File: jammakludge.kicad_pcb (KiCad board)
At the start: 2 copper layers, 31 parts, among them J1 Conn_02x28_Odd_Even, J2 Conn_02x28, J3 Conn_02x28

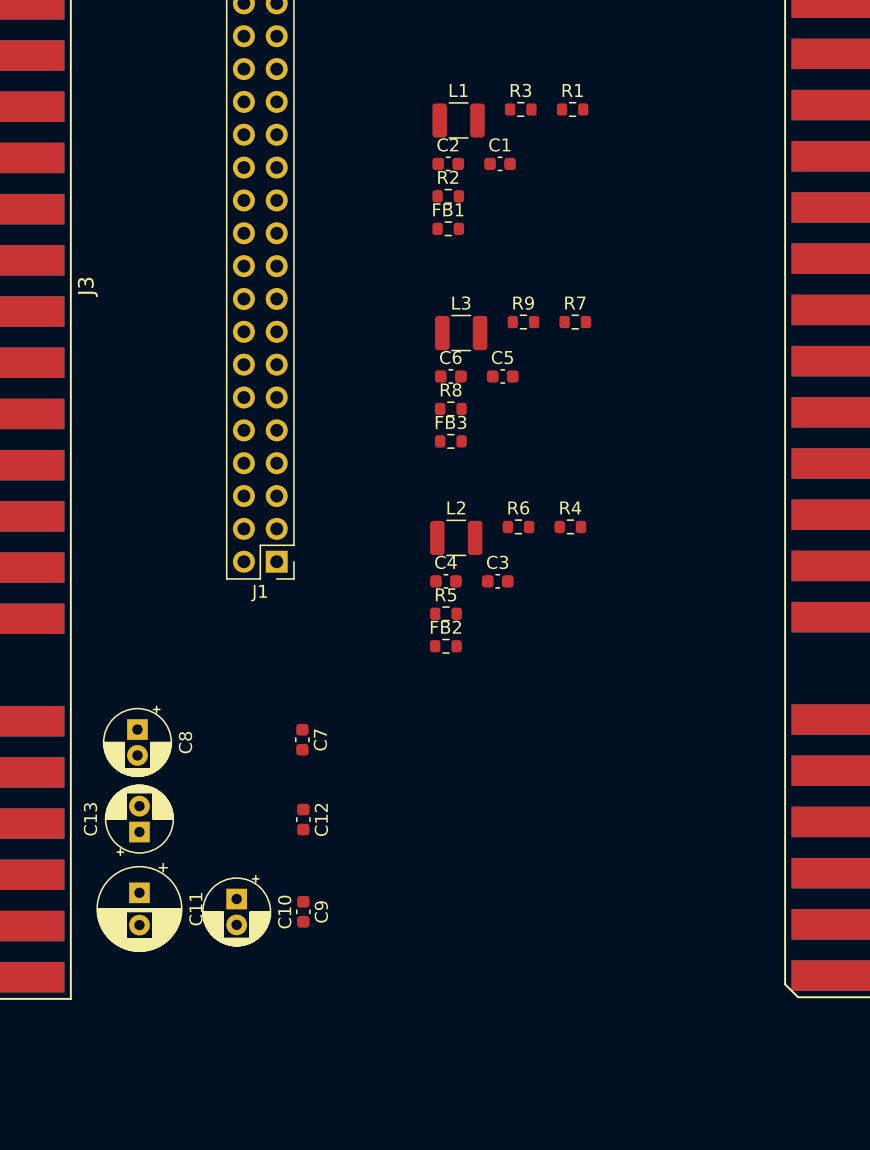
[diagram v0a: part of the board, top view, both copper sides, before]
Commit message: Added more power bypassing capacitors to 5v and 12v supplies.
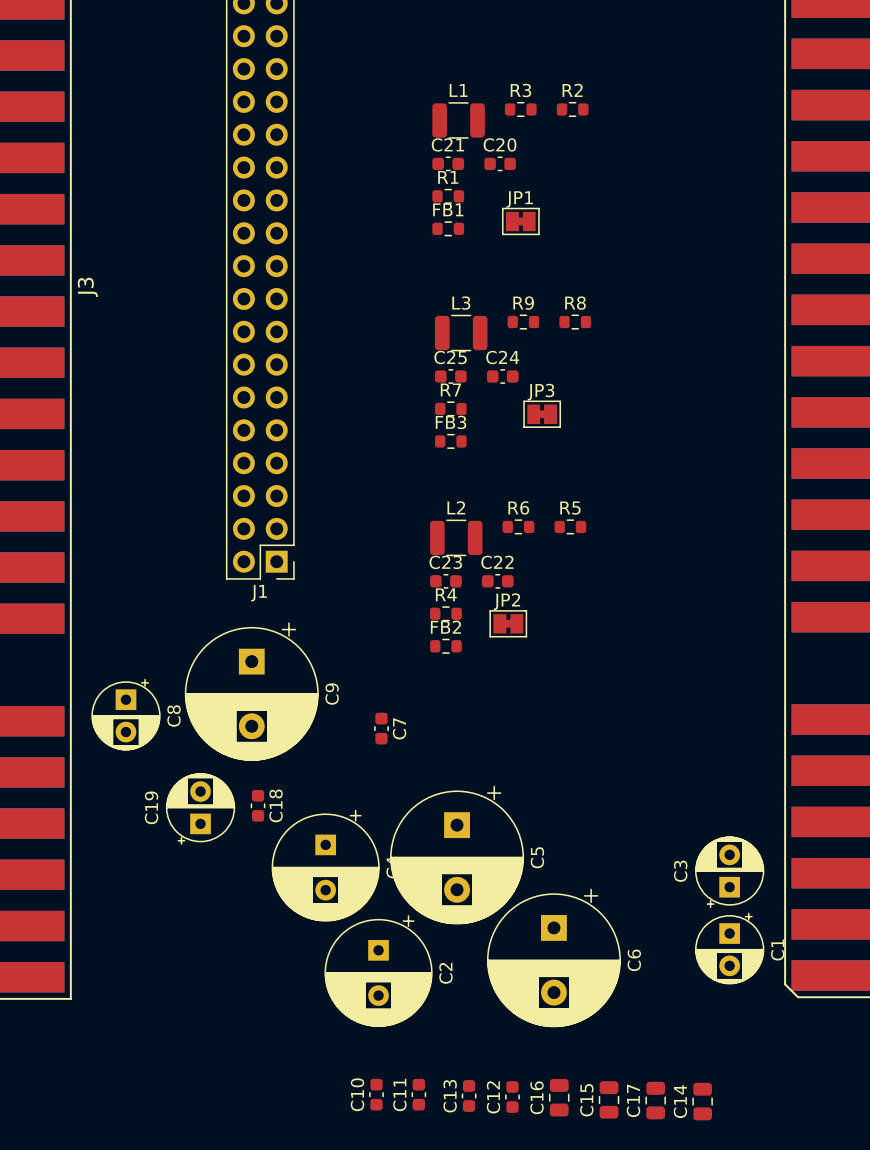
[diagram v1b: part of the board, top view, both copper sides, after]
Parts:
- added C11: C, Capacitor_SMD:C_0603_1608Metric, F.Cu at (56.3, 194.2)
- added C12: C, Capacitor_SMD:C_0603_1608Metric, F.Cu at (63.5, 194.4)
- added C13: C, Capacitor_SMD:C_0603_1608Metric, F.Cu at (60.2, 194.3)
- added C14: C, Capacitor_SMD:C_0805_2012Metric, F.Cu at (78.2, 194.7)
- added C15: C, Capacitor_SMD:C_0805_2012Metric, F.Cu at (71.0, 194.6)
- added C16: C, Capacitor_SMD:C_0805_2012Metric, F.Cu at (67.1, 194.4)
- added C17: C, Capacitor_SMD:C_0805_2012Metric, F.Cu at (74.6, 194.7)
- added C3: C_Polarized, Capacitor_THT:CP_Radial_D5.0mm_P2.50mm, F.Cu at (80.3, 178.2)
- added C4: C_Polarized, Capacitor_THT:CP_Radial_D8.0mm_P3.50mm, F.Cu at (49.1, 174.9)
- added C5: C_Polarized, Capacitor_THT:CP_Radial_D10.0mm_P5.00mm, F.Cu at (59.2, 173.4)
- added C6: C_Polarized, Capacitor_THT:CP_Radial_D10.0mm_P5.00mm, F.Cu at (66.7, 181.3)
- added C9: C_Polarized, Capacitor_THT:CP_Radial_D10.0mm_P5.00mm, F.Cu at (43.4, 160.7)
- added JP1: SolderJumper_2_Bridged, Jumper:SolderJumper-2_P1.3mm_Bridged_Pad1.0x1.5mm, F.Cu at (64.2, 126.7)
- added JP2: SolderJumper_2_Bridged, Jumper:SolderJumper-2_P1.3mm_Bridged_Pad1.0x1.5mm, F.Cu at (63.2, 157.8)
- added JP3: SolderJumper_2_Bridged, Jumper:SolderJumper-2_P1.3mm_Bridged_Pad1.0x1.5mm, F.Cu at (65.8, 141.6)
- C1: renamed from C10; footprint Capacitor_THT:CP_Radial_D5.0mm_P2.00mm -> Capacitor_THT:CP_Radial_D5.0mm_P2.50mm
- C19: renamed from C13; footprint Capacitor_THT:CP_Radial_D5.0mm_P2.00mm -> Capacitor_THT:CP_Radial_D5.0mm_P2.50mm
- C2: renamed from C11; footprint Capacitor_THT:CP_Radial_D6.3mm_P2.50mm -> Capacitor_THT:CP_Radial_D8.0mm_P3.50mm
- C8: footprint Capacitor_THT:CP_Radial_D5.0mm_P2.00mm -> Capacitor_THT:CP_Radial_D5.0mm_P2.50mm
- moved C1 38.2 mm to (80.3, 181.7)
- moved C2 19.0 mm to (53.2, 183.0)
- moved C10 15.2 mm to (53.0, 194.2), turned to 90 degrees
- moved C7 6.18 mm to (53.4, 165.9)
- moved C19 4.77 mm to (39.4, 173.3)
- moved C18 3.66 mm to (43.8, 171.9)
- moved C8 2.47 mm to (33.6, 163.7)
- renumbered C9 to C10, C12 to C18, C1 to C20, C2 to C21, C3 to C22, C4 to C23, C5 to C24, C6 to C25, R2 to R1, R1 to R2, R5 to R4, R4 to R5, R8 to R7, R7 to R8

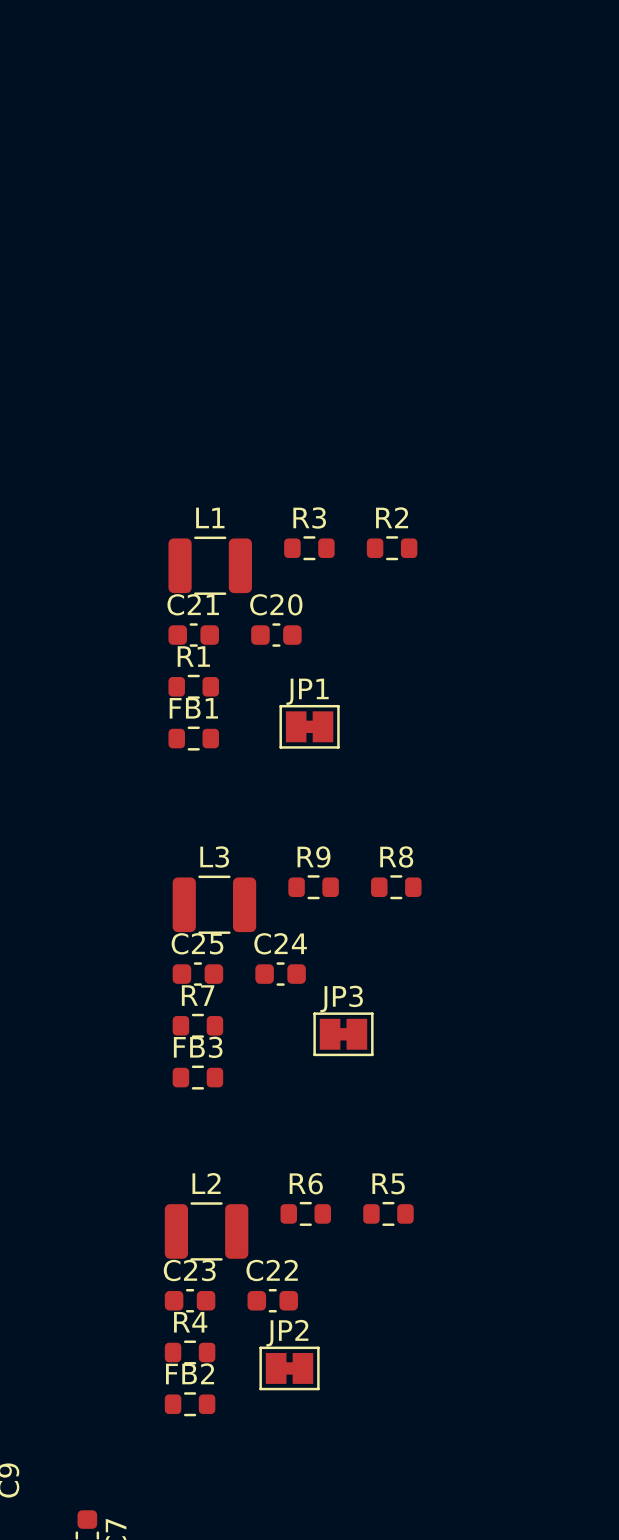
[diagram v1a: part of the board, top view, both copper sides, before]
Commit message: Added test points/breakout points for video filter input and output
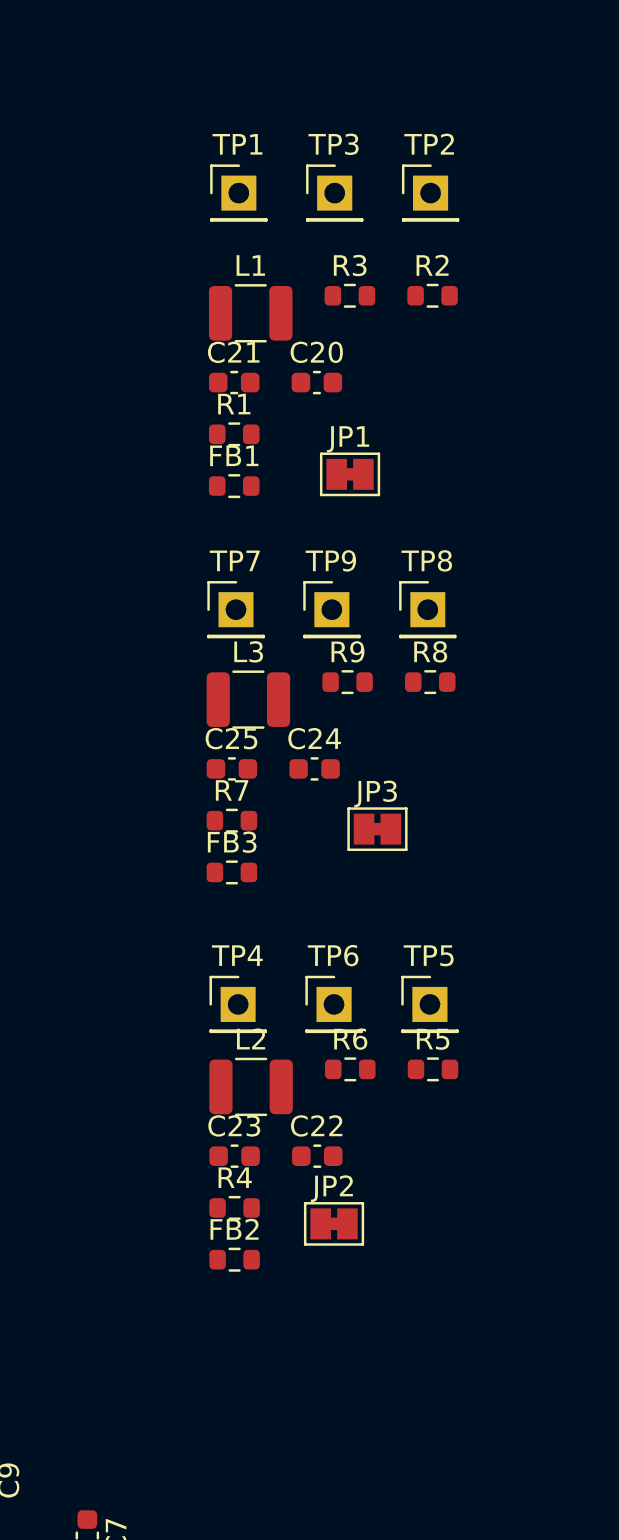
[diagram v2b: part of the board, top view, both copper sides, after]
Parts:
- added TP1: TestPoint, Connector_PinHeader_2.54mm:PinHeader_1x01_P2.54mm_Vertical, F.Cu at (60.7, 100.8)
- added TP2: TestPoint, Connector_PinHeader_2.54mm:PinHeader_1x01_P2.54mm_Vertical, F.Cu at (70.0, 100.8)
- added TP3: TestPoint, Connector_PinHeader_2.54mm:PinHeader_1x01_P2.54mm_Vertical, F.Cu at (65.4, 100.8)
- added TP4: TestPoint, Connector_PinHeader_2.54mm:PinHeader_1x01_P2.54mm_Vertical, F.Cu at (60.7, 140.1)
- added TP5: TestPoint, Connector_PinHeader_2.54mm:PinHeader_1x01_P2.54mm_Vertical, F.Cu at (70.0, 140.1)
- added TP6: TestPoint, Connector_PinHeader_2.54mm:PinHeader_1x01_P2.54mm_Vertical, F.Cu at (65.4, 140.1)
- added TP7: TestPoint, Connector_PinHeader_2.54mm:PinHeader_1x01_P2.54mm_Vertical, F.Cu at (60.6, 121.0)
- added TP8: TestPoint, Connector_PinHeader_2.54mm:PinHeader_1x01_P2.54mm_Vertical, F.Cu at (69.9, 121.0)
- added TP9: TestPoint, Connector_PinHeader_2.54mm:PinHeader_1x01_P2.54mm_Vertical, F.Cu at (65.2, 121.0)
- moved C20 12.4 mm to (64.5, 110.0)
- moved C21 12.4 mm to (60.5, 110.0)
- moved FB1 12.4 mm to (60.5, 115.0)
- moved L1 12.4 mm to (61.3, 106.6)
- moved JP1 12.4 mm to (66.1, 114.4)
- moved R1 12.4 mm to (60.5, 112.5)
- moved R2 12.4 mm to (70.1, 105.8)
- moved R3 12.4 mm to (66.1, 105.8)
- moved C25 10.1 mm to (60.4, 128.7)
- moved FB3 10.1 mm to (60.4, 133.7)
- moved R7 10.1 mm to (60.4, 131.2)
- moved R9 10.1 mm to (66.0, 124.5)
- moved C24 10.1 mm to (64.4, 128.7)
- moved JP3 10.1 mm to (67.5, 131.6)
- moved L3 10.1 mm to (61.2, 125.4)
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
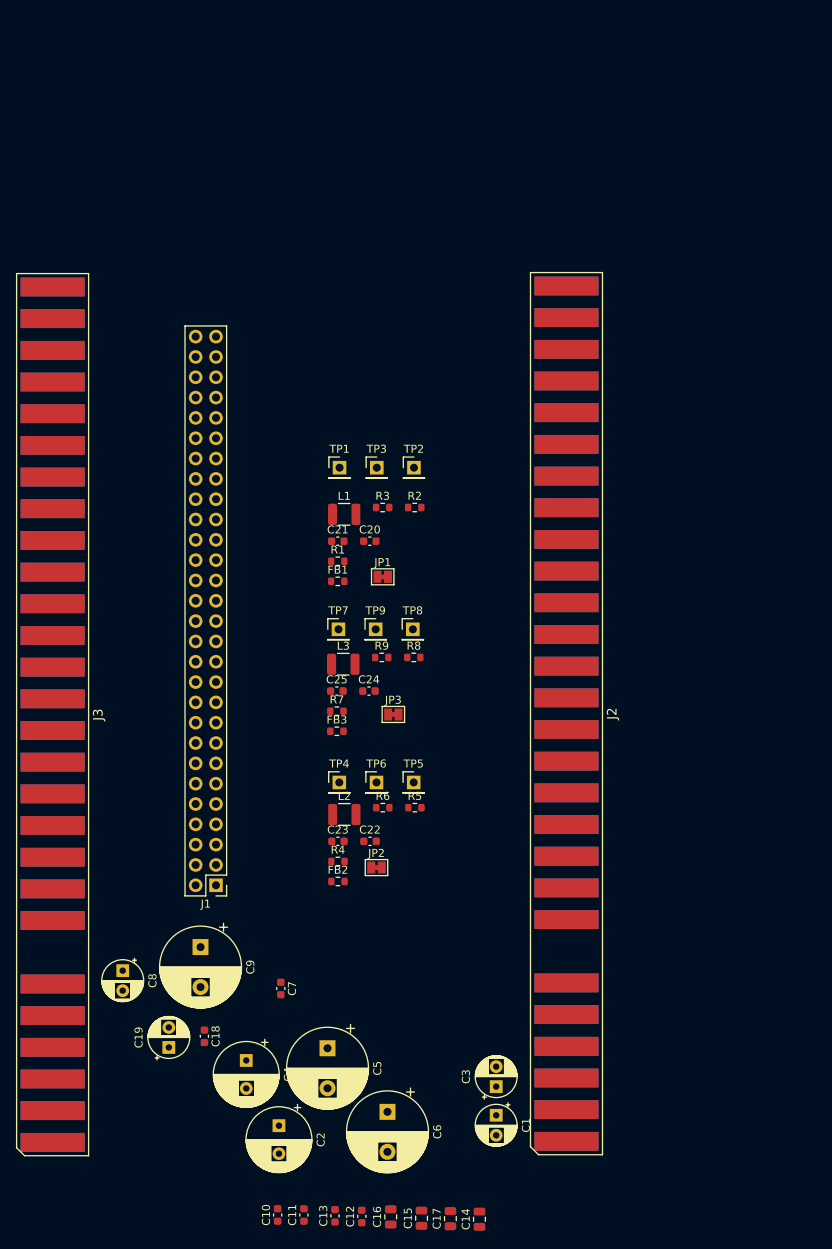
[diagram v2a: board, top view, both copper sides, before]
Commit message: Mostly completed layout, fixed some labels that didn't match right. Left to do: better gnd stitching and tidy up
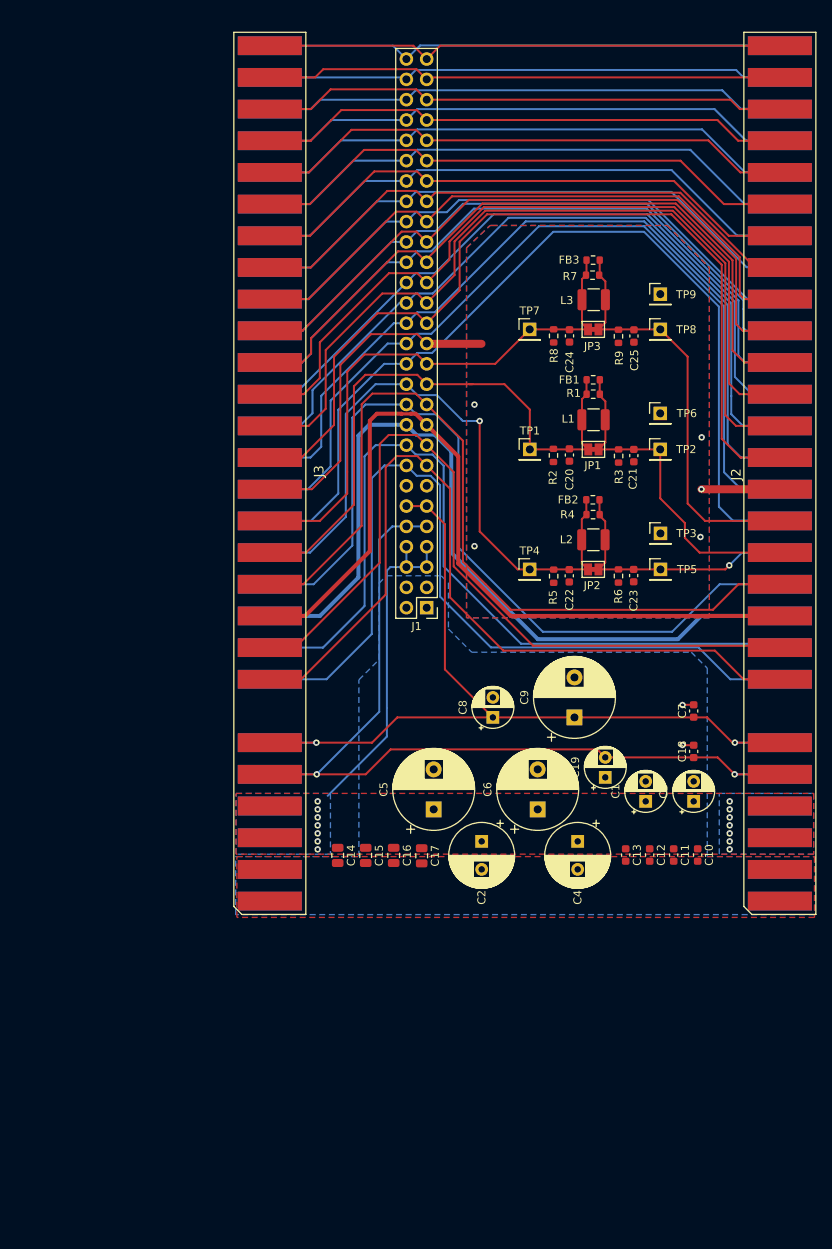
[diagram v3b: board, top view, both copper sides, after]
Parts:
- moved C18 70.8 mm to (105.0, 136.2), turned to 90 degrees
- moved C10 69.1 mm to (105.5, 149.2), turned to -90 degrees
- moved FB3 67.0 mm to (92.4, 74.8)
- moved C11 64.5 mm to (102.5, 149.2), turned to -90 degrees
- moved C19 64.2 mm to (94.0, 139.5)
- moved R7 63.2 mm to (92.4, 76.7)
- moved C7 62.2 mm to (105.0, 131.2), turned to 90 degrees
- moved TP6 58.2 mm to (100.8, 94.0)
- moved C13 57.9 mm to (96.5, 149.2), turned to -90 degrees
- moved C25 57.9 mm to (97.5, 84.3), turned to -90 degrees
- moved C12 57.8 mm to (99.5, 149.2), turned to -90 degrees
- moved FB2 57.4 mm to (92.4, 104.8)
- moved C8 56.1 mm to (79.9, 132.0), turned to 90 degrees
- moved L3 55.3 mm to (92.5, 79.8)
- moved TP9 55.0 mm to (100.8, 79.1)
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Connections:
- net /VideoGnd renamed /VidGnd
- FB1 pad 1: /VidRedIn -> (no net)
- FB1 pad 2: /VidRed -> (no net)
- J1 pad 15: Net-(J1-Pad15) -> /Meter_1
- J1 pad 16: Net-(J1-Pad16) -> /Meter_2
- J1 pad 17: Net-(J1-Pad17) -> /Lockout_1
- J1 pad 18: Net-(J1-Pad18) -> /Lockout_2
- J1 pad 19: Net-(J1-Pad19) -> /Speaker_+
- J1 pad 20: Net-(J1-Pad20) -> /Speaker_-
- J1 pad 21: Net-(J1-Pad21) -> /Audio_+
- J1 pad 22: Net-(J1-Pad22) -> /Audio_gnd
- J1 pad 23: /VidRed -> /VidRedIn
- J1 pad 24: /VidGreen -> /VidGreenIn
- J1 pad 25: /VidBlue -> /VidBlueIn
- J1 pad 26: Net-(J1-Pad26) -> /VidSync
- J1 pad 28: Net-(J1-Pad28) -> /Service_switch
- J1 pad 29: Net-(J1-Pad29) -> /Test_switch
- J1 pad 30: Net-(J1-Pad30) -> /Tilt_switch
- J1 pad 31: Net-(J1-Pad31) -> /Coin_1
- J1 pad 32: Net-(J1-Pad32) -> /Coin_2
- J1 pad 33: Net-(J1-Pad33) -> /P1_start
- J1 pad 34: Net-(J1-Pad34) -> /P2_start
- J1 pad 35: Net-(J1-Pad35) -> /P1_up
- J1 pad 36: Net-(J1-Pad36) -> /P2_up
- J1 pad 37: Net-(J1-Pad37) -> /P1_down
- J1 pad 38: Net-(J1-Pad38) -> /P2_down
- J1 pad 39: Net-(J1-Pad39) -> /P1_left
- J1 pad 40: Net-(J1-Pad40) -> /P2_left
- J1 pad 41: Net-(J1-Pad41) -> /P1_right
- J1 pad 42: Net-(J1-Pad42) -> /P2_right
- J1 pad 43: Net-(J1-Pad43) -> /P1_button1
- J1 pad 44: Net-(J1-Pad44) -> /P2_button1
- J1 pad 45: Net-(J1-Pad45) -> /P1_button2
- J1 pad 46: Net-(J1-Pad46) -> /P2_button2
- J1 pad 47: Net-(J1-Pad47) -> /P1_button3
- J1 pad 48: Net-(J1-Pad48) -> /P2_button3
- J1 pad 49: Net-(J1-Pad49) -> /P1_button4
- J1 pad 50: Net-(J1-Pad50) -> /P2_button4
- J1 pad 51: Net-(J1-Pad51) -> /Nc_26
- J1 pad 52: Net-(J1-Pad52) -> /Nc_d
- J1 pad 53: Net-(J1-Pad53) -> /Gnd_27
- J1 pad 54: Net-(J1-Pad54) -> /Gnd_e
- J1 pad 55: Net-(J1-Pad55) -> /Gnd_28
- J1 pad 56: Net-(J1-Pad56) -> /Gnd_f
- J2 pad 10: Net-(J2-Pad10) -> /Speaker_+
- J2 pad 11: Net-(J2-Pad11) -> /Audio_+
- J2 pad 12: /VidRedIn -> /VidRed
- J2 pad 13: /VidBlueIn -> /VidBlue
- J2 pad 15: Net-(J2-Pad15) -> /Test_switch
- J2 pad 16: Net-(J2-Pad16) -> /Coin_1
- J2 pad 17: Net-(J2-Pad17) -> /P1_start
- J2 pad 18: Net-(J2-Pad18) -> /P1_up
- J2 pad 19: Net-(J2-Pad19) -> /P1_down
- J2 pad 20: Net-(J2-Pad20) -> /P1_left
- J2 pad 21: Net-(J2-Pad21) -> /P1_right
- J2 pad 22: Net-(J2-Pad22) -> /P1_button1
- J2 pad 23: Net-(J2-Pad23) -> /P1_button2
- J2 pad 24: Net-(J2-Pad24) -> /P1_button3
- J2 pad 25: Net-(J2-Pad25) -> /P1_button4
- J2 pad 26: Net-(J2-Pad26) -> /Nc_26
- J2 pad 27: Net-(J2-Pad27) -> /Gnd_27
- J2 pad 28: Net-(J2-Pad28) -> /Gnd_28
- J2 pad 8: Net-(J2-Pad8) -> /Meter_1
- J2 pad 9: Net-(J2-Pad9) -> /Lockout_1
- J2 pad J: Net-(J2-PadJ) -> /Meter_2
- J2 pad K: Net-(J2-PadK) -> /Lockout_2
- J2 pad L: Net-(J2-PadL) -> /Speaker_-
- J2 pad M: Net-(J2-PadM) -> /Audio_gnd
- J2 pad N: /VidGreenIn -> /VidGreen
- J2 pad P: Net-(J2-PadP) -> /VidSync
- J2 pad R: Net-(J2-PadR) -> /Service_switch
- J2 pad S: Net-(J2-PadS) -> /Tilt_switch
- J2 pad T: Net-(J2-PadT) -> /Coin_2
- J2 pad U: Net-(J2-PadU) -> /P2_start
- J2 pad V: Net-(J2-PadV) -> /P2_up
- J2 pad W: Net-(J2-PadW) -> /P2_down
- J2 pad X: Net-(J2-PadX) -> /P2_left
- J2 pad Y: Net-(J2-PadY) -> /P2_right
- J2 pad Z: Net-(J2-PadZ) -> /P2_button1
- J2 pad a: Net-(J2-Pada) -> /P2_button2
- J2 pad b: Net-(J2-Padb) -> /P2_button3
- J2 pad c: Net-(J2-Padc) -> /P2_button4
- J2 pad d: Net-(J2-Padd) -> /Nc_d
- J2 pad e: Net-(J2-Pade) -> /Gnd_e
- J2 pad f: Net-(J2-Padf) -> /Gnd_f
- J3 pad 10: Net-(J3-Pad10) -> /Speaker_+
- J3 pad 11: Net-(J3-Pad11) -> /Audio_+
- J3 pad 12: /VidRed -> /VidRedIn
- J3 pad 13: /VidBlue -> /VidBlueIn
- J3 pad 15: Net-(J3-Pad15) -> /Test_switch
- J3 pad 16: Net-(J3-Pad16) -> /Coin_1
- J3 pad 17: Net-(J3-Pad17) -> /P1_start
- J3 pad 18: Net-(J3-Pad18) -> /P1_up
- J3 pad 19: Net-(J3-Pad19) -> /P1_down
- J3 pad 20: Net-(J3-Pad20) -> /P1_left
- J3 pad 21: Net-(J3-Pad21) -> /P1_right
- J3 pad 22: Net-(J3-Pad22) -> /P1_button1
- J3 pad 23: Net-(J3-Pad23) -> /P1_button2
- J3 pad 24: Net-(J3-Pad24) -> /P1_button3
- J3 pad 25: Net-(J3-Pad25) -> /P1_button4
- J3 pad 26: Net-(J3-Pad26) -> /Nc_26
- J3 pad 27: Net-(J3-Pad27) -> /Gnd_27
- J3 pad 28: Net-(J3-Pad28) -> /Gnd_28
- J3 pad 8: Net-(J3-Pad8) -> /Meter_1
- J3 pad 9: Net-(J3-Pad9) -> /Lockout_1
- J3 pad J: Net-(J3-PadJ) -> /Meter_2
- J3 pad K: Net-(J3-PadK) -> /Lockout_2
- J3 pad L: Net-(J3-PadL) -> /Speaker_-
- J3 pad M: Net-(J3-PadM) -> /Audio_gnd
- J3 pad N: /VidGreen -> /VidGreenIn
- J3 pad P: Net-(J3-PadP) -> /VidSync
- J3 pad R: Net-(J3-PadR) -> /Service_switch
- J3 pad S: Net-(J3-PadS) -> /Tilt_switch
- J3 pad T: Net-(J3-PadT) -> /Coin_2
- J3 pad U: Net-(J3-PadU) -> /P2_start
- J3 pad V: Net-(J3-PadV) -> /P2_up
- J3 pad W: Net-(J3-PadW) -> /P2_down
- J3 pad X: Net-(J3-PadX) -> /P2_left
- J3 pad Y: Net-(J3-PadY) -> /P2_right
- J3 pad Z: Net-(J3-PadZ) -> /P2_button1
- J3 pad a: Net-(J3-Pada) -> /P2_button2
- J3 pad b: Net-(J3-Padb) -> /P2_button3
- J3 pad c: Net-(J3-Padc) -> /P2_button4
- J3 pad d: Net-(J3-Padd) -> /Nc_d
- J3 pad e: Net-(J3-Pade) -> /Gnd_e
- J3 pad f: Net-(J3-Padf) -> /Gnd_f
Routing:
- net -5V: track 0.00 -> 117.1 mm, vias 0 -> 2
- net /VidSync: track 0.00 -> 114.5 mm
- net /Test_switch: track 0.00 -> 111.3 mm
- net +12V: track 0.00 -> 110.5 mm, vias 0 -> 2
- net /Service_switch: track 0.00 -> 107.9 mm
- net /Meter_2: track 0.00 -> 105.5 mm
- net /Coin_1: track 0.00 -> 104.9 mm
- net /Audio_gnd: track 0.00 -> 104.7 mm
- net /Meter_1: track 0.00 -> 104.2 mm
- net /Audio_+: track 0.00 -> 103.9 mm
- net /Speaker_-: track 0.00 -> 103.7 mm
- net /Lockout_2: track 0.00 -> 103.0 mm
- net /Tilt_switch: track 0.00 -> 102.1 mm
- net /Speaker_+: track 0.00 -> 102.1 mm
- net /Lockout_1: track 0.00 -> 101.4 mm
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- added copper zone on B.Cu, net +5V
- added copper zone on F.Cu, net +5V
- added copper zone on B.Cu, net /VidGnd
- added copper zone on F.Cu, net /VidGnd
- added copper zone on B.Cu, net GND
- added copper zone on F.Cu, net GND
